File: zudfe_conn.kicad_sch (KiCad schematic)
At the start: 3 parts, among them J1 6469028-1, J2 6469028-1, J3 6469028-1

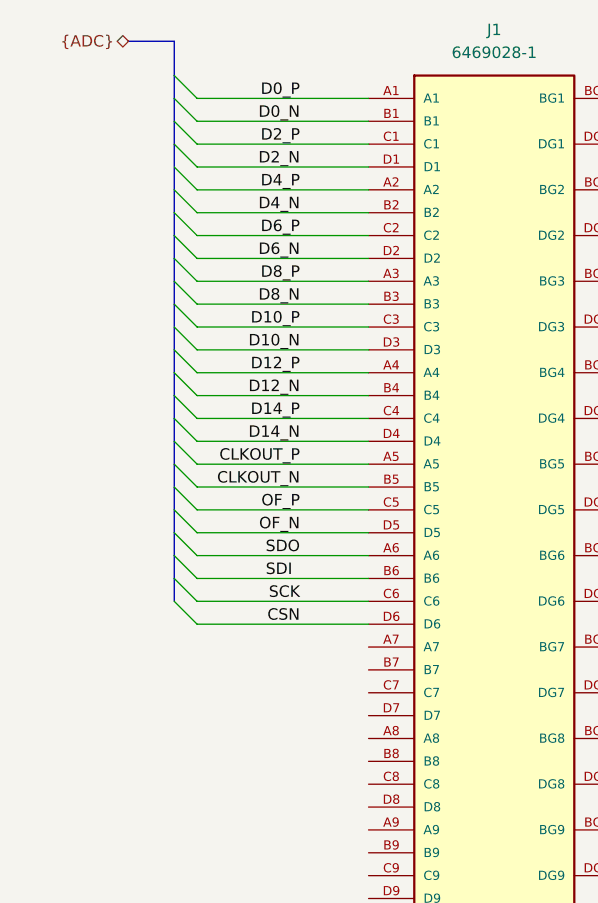
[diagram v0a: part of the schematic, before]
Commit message: Untangled adc data connections
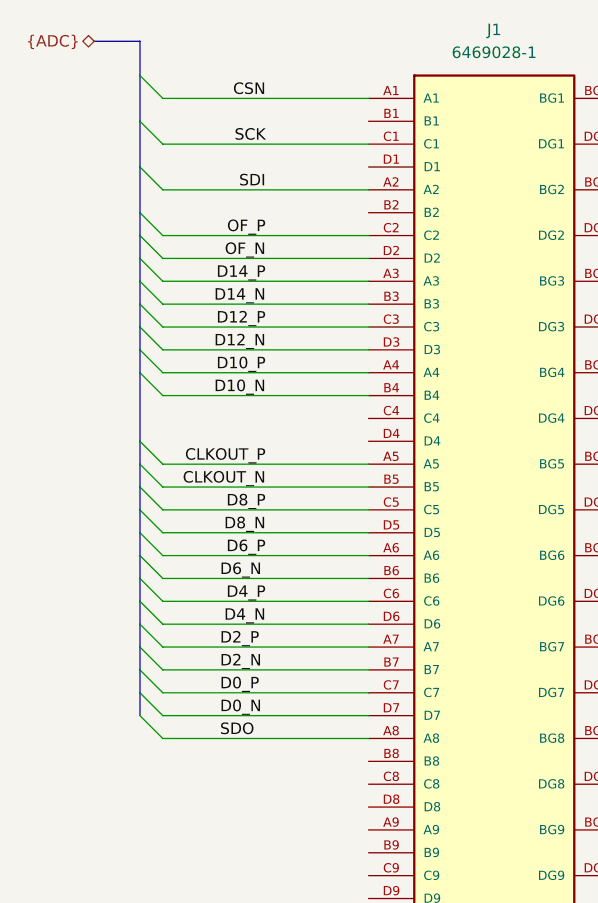
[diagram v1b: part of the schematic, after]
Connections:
- net CSN: now also J1.A1; no longer J1.D6
- net D0_N: now also J1.D7; no longer J1.B1
- net D0_P: now also J1.C7; no longer J1.A1
- net D10_N: now also J1.B4; no longer J1.D3
- net D10_P: now also J1.A4; no longer J1.C3
- net D12_N: now also J1.D3; no longer J1.B4
- net D12_P: now also J1.C3; no longer J1.A4
- net D14_N: now also J1.B3; no longer J1.D4
- net D14_P: now also J1.A3; no longer J1.C4
- net D2_N: now also J1.B7; no longer J1.D1
- net D2_P: now also J1.A7; no longer J1.C1
- net D4_N: now also J1.D6; no longer J1.B2
- net D4_P: now also J1.C6; no longer J1.A2
- net D6_N: now also J1.B6; no longer J1.D2
- net D6_P: now also J1.A6; no longer J1.C2
- net D8_N: now also J1.D5; no longer J1.B3
- net D8_P: now also J1.C5; no longer J1.A3
- net OF_N: now also J1.D2; no longer J1.D5
- net OF_P: now also J1.C2; no longer J1.C5
- net SCK: now also J1.C1; no longer J1.C6
- net SDI: now also J1.A2; no longer J1.B6
- net SDO: now also J1.A8; no longer J1.A6

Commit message: Finish routing
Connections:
- net fault_led0: now also J2.D10; no longer J2.A1
- net fault_led1: now also J2.C10; no longer J2.B1
- net fault_led10: now also J2.D5; no longer J2.C3
- net fault_led11: now also J2.C5; no longer J2.D3
- net fault_led12: now also J2.D4; no longer J2.A4
- net fault_led13: now also J2.C4; no longer J2.B4
- net fault_led14: now also J2.D3; no longer J2.C4
- net fault_led15: now also J2.C3; no longer J2.D4
- net fault_led2: now also J2.D9; no longer J2.C1
- net fault_led3: now also J2.C9; no longer J2.D1
- net fault_led4: now also J2.D8; no longer J2.A2
- net fault_led5: now also J2.C8; no longer J2.B2
- net fault_led6: now also J2.D7; no longer J2.C2
- net fault_led7: now also J2.C7; no longer J2.D2
- net fault_led8: now also J2.D6; no longer J2.A3
- net fault_led9: now also J2.C6; no longer J2.B3
- net fault_rdbk: now also J3.D9; no longer J3.A8
- net fault_reset: now also J3.C9; no longer J3.B8
- net faultn: now also J3.A10; no longer J3.D7
- net force_trip: now also J3.B9; no longer J3.C8
- net keylock: now also J3.A9; no longer J3.D8
- net spare0: now also J3.D8; no longer J3.A9
- net spare1: now also J3.C8; no longer J3.B9
- net spare2: now also J3.B8; no longer J3.C9
- net spare3: now also J3.A8; no longer J3.D9
- net spare4: now also J3.D7; no longer J3.A10
- net tp_neg0: now also J3.A2; no longer J3.B2
- net tp_neg1: now also J3.D1; no longer J3.C2
- net tp_neg2: now also J3.C1; no longer J3.D2
- net tp_neg3: now also J3.B1; no longer J3.A3
- net tp_neg4: now also J3.A1; no longer J3.B3
- net tp_pos0: now also J3.B3; no longer J3.A1
- net tp_pos1: now also J3.A3; no longer J3.B1
- net tp_pos2: now also J3.D2; no longer J3.C1
- net tp_pos3: now also J3.C2; no longer J3.D1
- net tp_pos4: now also J3.B2; no longer J3.A2

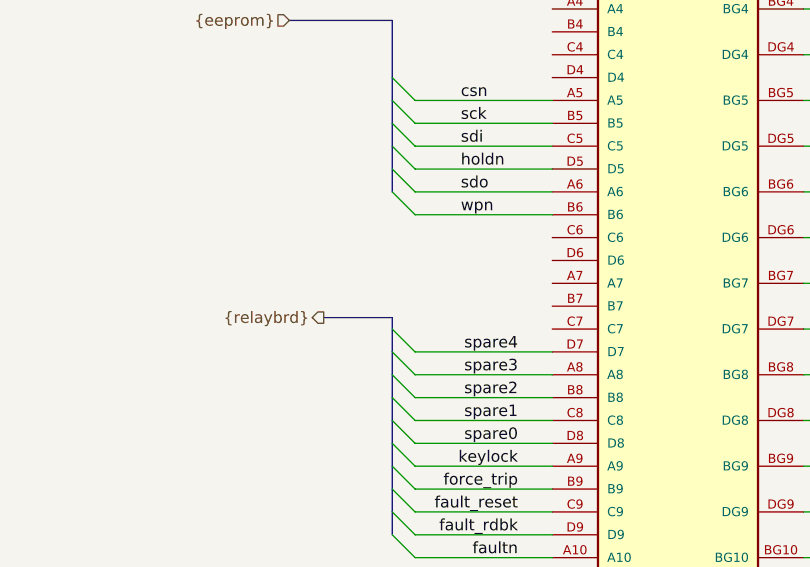
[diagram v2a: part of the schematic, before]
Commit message: Add watchdog window IC
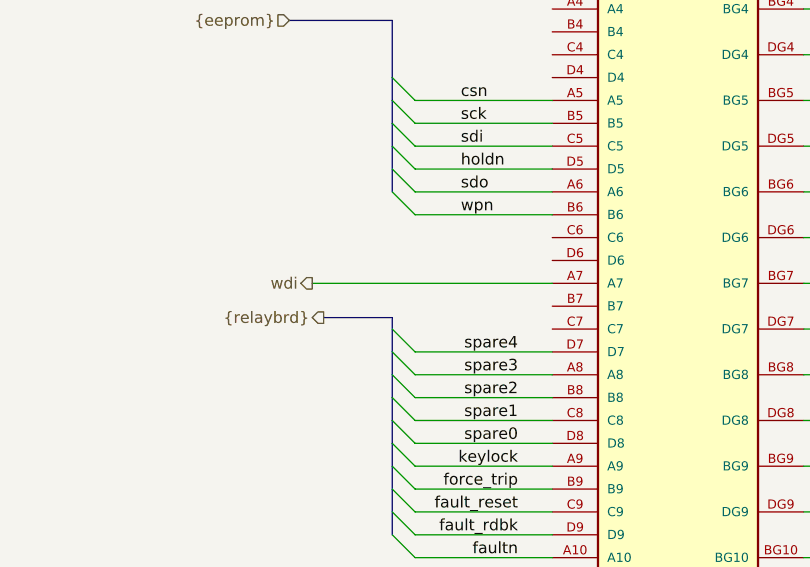
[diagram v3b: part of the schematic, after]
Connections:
- net wdi: now reaches J3.A7
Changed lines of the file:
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@@
+	(wire
+		(pts
+			(xy 311.15 135.89) (xy 337.82 135.89)
+		)
+		(stroke
+			(width 0)
+			(type default)
+		)
+	)
 	(wire
 		(pts
@@
 		(effects
 			(font
+				(size 1.27 1.27)
+			)
+			(justify right)
+		)
+	)
+	(hierarchical_label "wdi"
+		(shape output)
+		(at 311.15 135.89 180)
+		(effects
+			(font
